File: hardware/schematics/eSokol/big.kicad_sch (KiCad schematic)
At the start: 35 parts, among them J2 MOT_DRV_THR, J3 THR_JACK, J4 THR_JACK, J6 BIGBATT_CHRG, J7 MOT_DRV_THR, M1 MY1016Z2, M2 Fan, Q11 BC547, Q12 S8550, Q13 BC547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

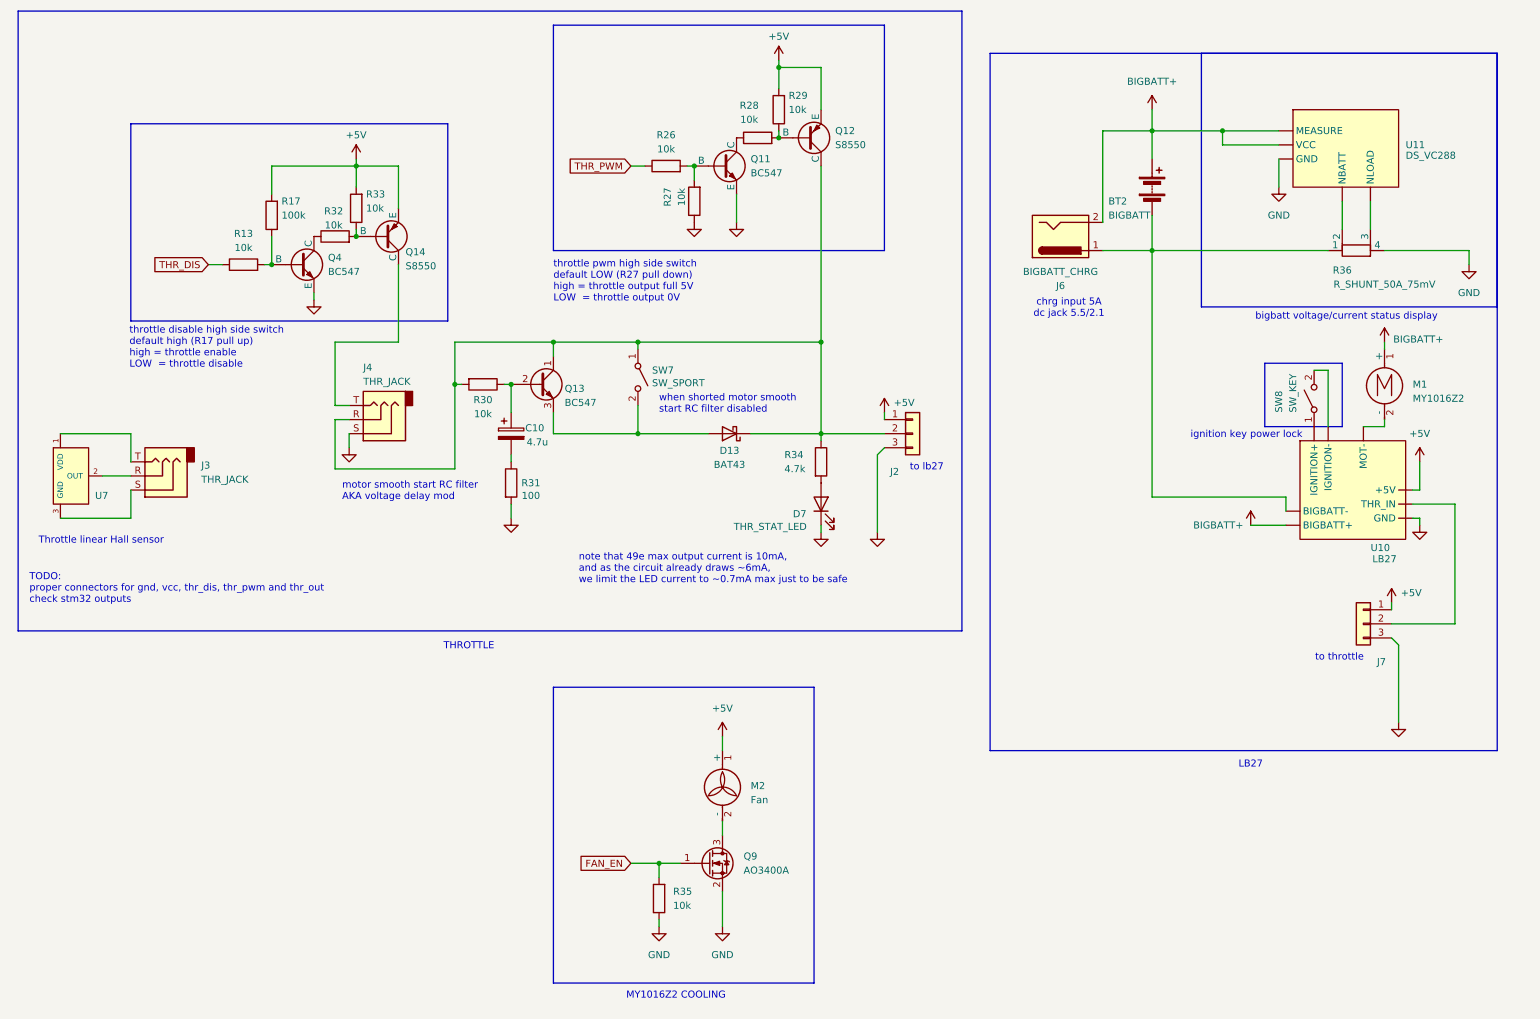
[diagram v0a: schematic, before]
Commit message: Create one BIG schematic containing everything related to motor and its driver
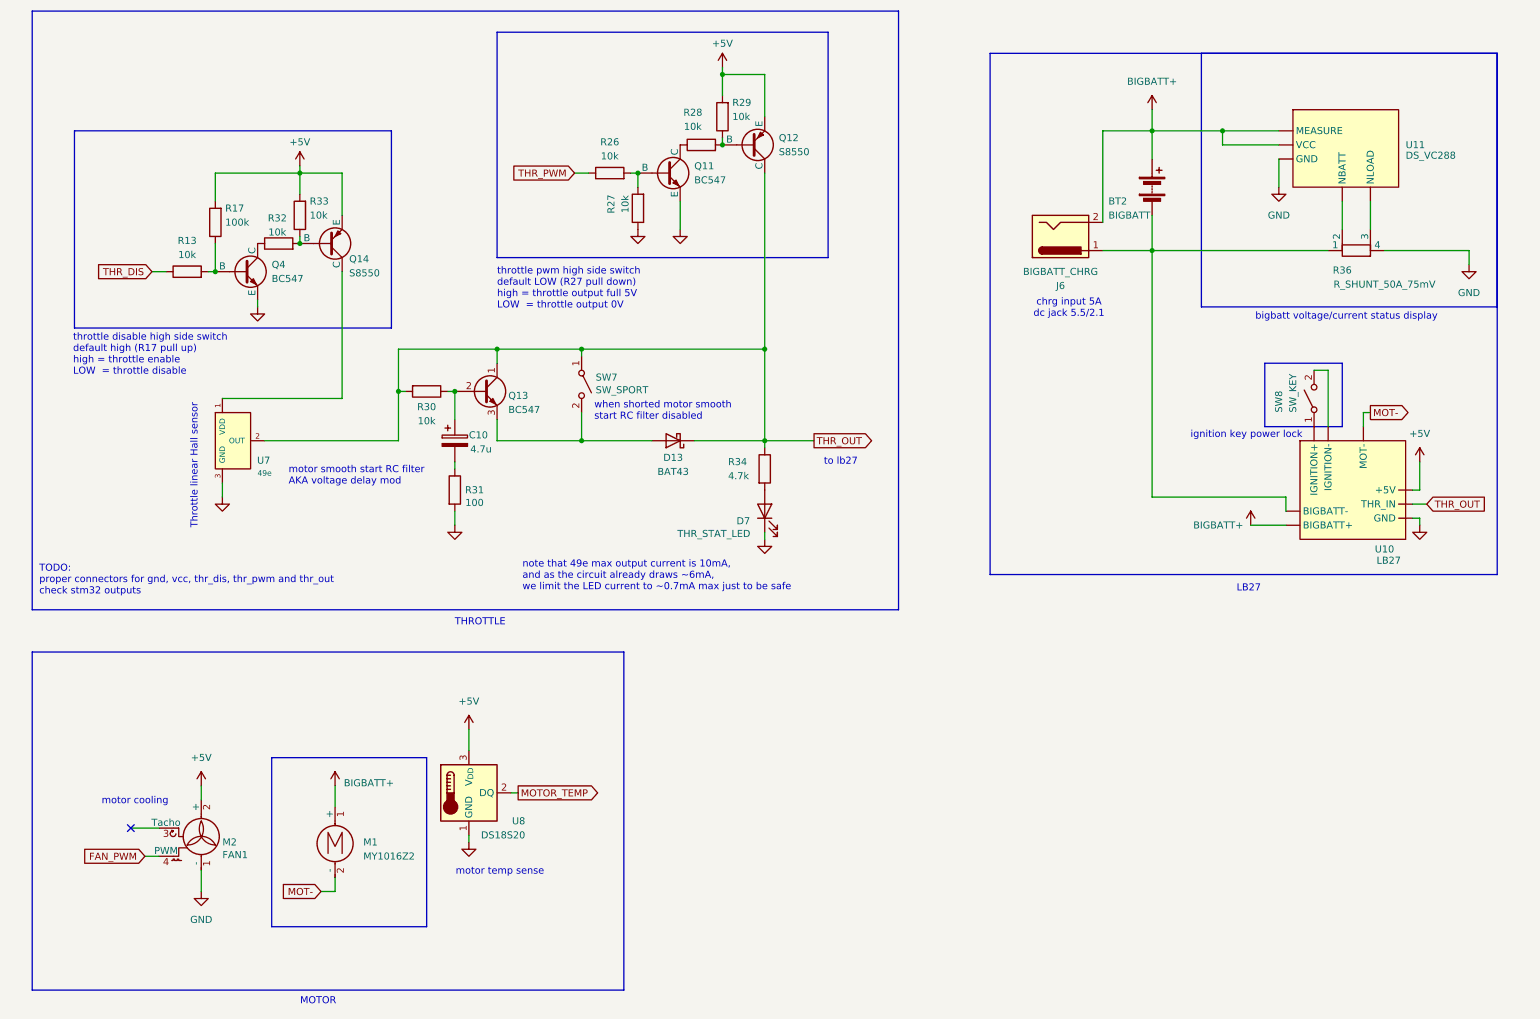
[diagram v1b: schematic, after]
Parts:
- removed J2, J7: MOT_DRV_THR, symbol Connector_Generic:Conn_01x03
- removed J3, J4: THR_JACK, symbol Connector_Audio:AudioJack3
- removed M2: Fan, symbol Motor:Fan
- removed Q9: AO3400A, Package_TO_SOT_SMD:SOT-23, symbol Transistor_FET:AO3400A
- removed R35: 10k, symbol Device:R
- added M2: FAN1, symbol Motor:Fan_4pin
- added U8: DS18S20, Package_TO_SOT_THT:TO-92_Inline, symbol Sensor_Temperature:DS18S20
- U7: value Hall_Sensor -> 49e
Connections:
- net +5V: now also M2.2 (+), U8.3 (V_{DD})
- net GND: now also U7.3 (GND), M2.1 (-), U8.1 (GND)
- net THR_OUT: now reaches D13.1 (K), Q12.1 (C), Q13.1 (C), R30.2, R34.1, SW7.1 (A)
- net THR_OUT: now also U10. (THR_IN), U7.2 (OUT)
- net at Q14.1 (C): now also U7.1 (VDD)
- net MOT-: now reaches M1.2 (-), U10. (THR_IN)
- new net FAN_PWM: M2.4 (PWM)
- new net MOTOR_TEMP: U8.2 (DQ)
- no-connect marks 0 -> 1
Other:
- note added: "MOTOR"
- note added: "motor cooling"
- note added: "motor temp sense"
- note removed: "MY1016Z2 COOLING"
- note removed: "to throttle"
- moved on the sheet: C10, D13, D7, Q11, Q12, Q13, Q14, Q4, R13, R17, R26, R27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

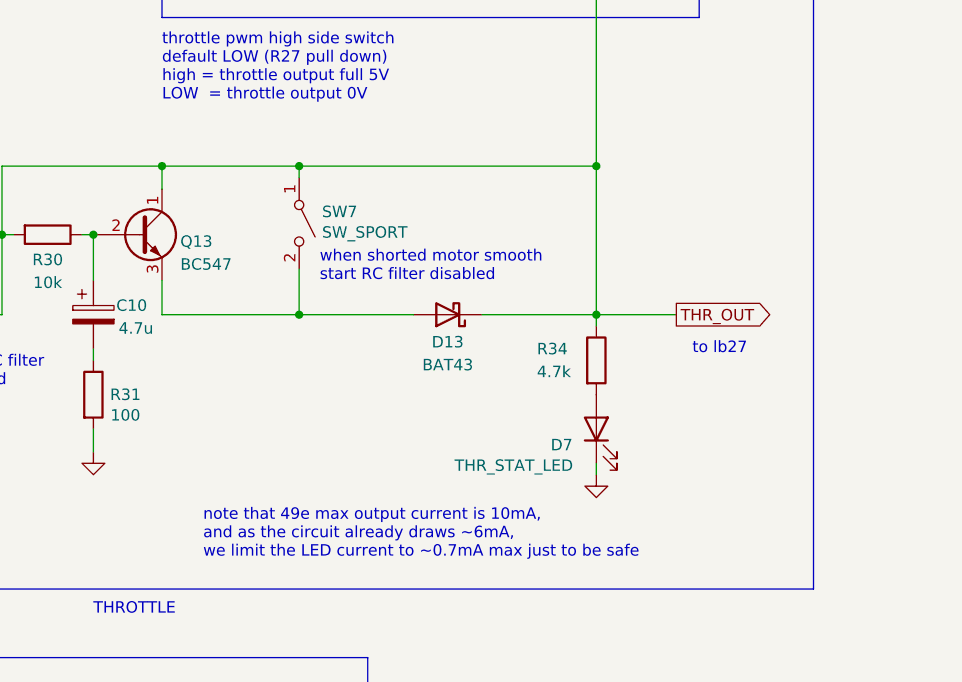
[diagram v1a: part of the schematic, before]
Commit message: schematics: eSokol: big: replace SW_SPORT with digital THR_SPORT input
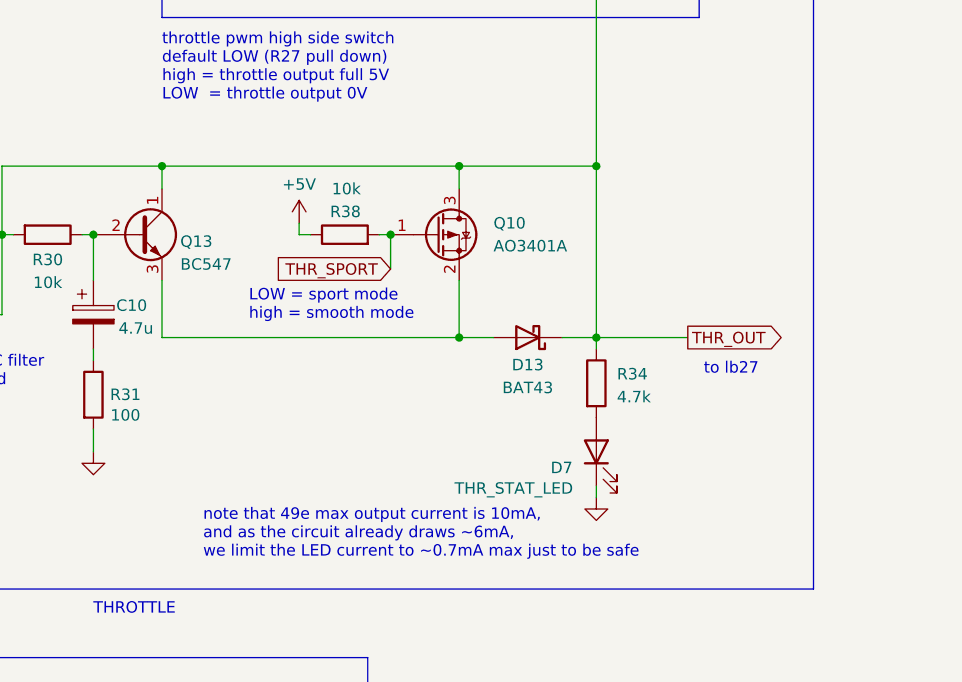
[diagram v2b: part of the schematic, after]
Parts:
- removed SW7: SW_SPORT, Button_Switch_THT:SW_DIP_SPSTx01_Slide_9.78x4.72mm_W7.62mm_P2.54mm, symbol Switch:SW_SPST
- added Q10: AO3401A, Package_TO_SOT_SMD:SOT-23, symbol Transistor_FET:AO3401A
- added R38: 10k, symbol Device:R
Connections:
- net +5V: now also R38.1
- net THR_OUT: now also Q10.3 (D)
- net at D13.2 (A), Q13.3 (E): now also Q10.2 (S)
- new net THR_SPORT: Q10.1 (G), R38.2
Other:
- note added: "LOW = sport mode high = smooth mode"
- note removed: "when shorted motor smooth start RC filter disabled"
- moved on the sheet: D13, D7, R34

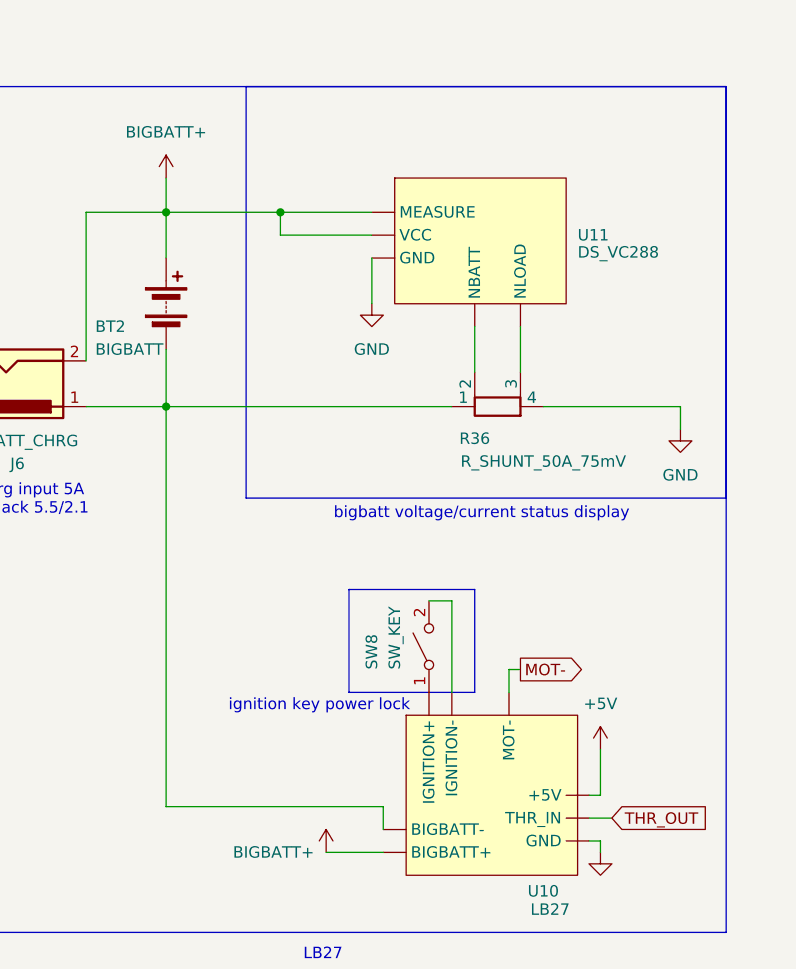
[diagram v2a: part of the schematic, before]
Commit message: hardware/schematics: update mcu and big schematics to reflect current project state
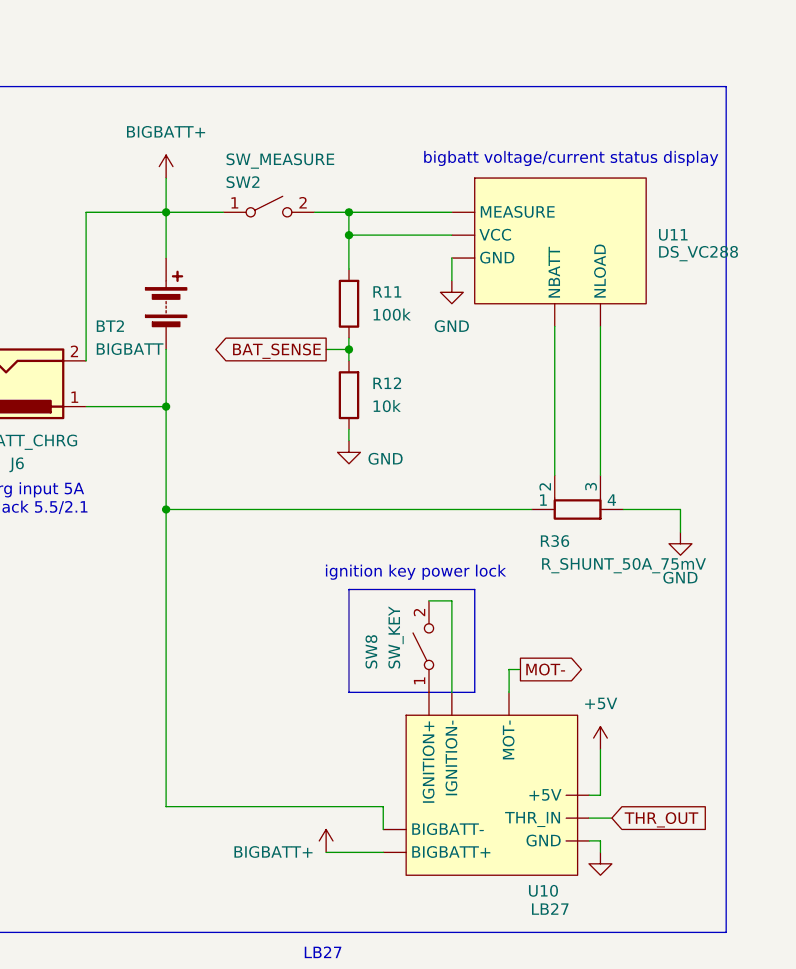
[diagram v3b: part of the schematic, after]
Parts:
- added R11: 100k, symbol Device:R
- added R12: 10k, symbol Device:R
- added SW2: SW_MEASURE, symbol Switch:SW_SPST
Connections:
- net BIGBATT+: now also SW2.1 (A); no longer U11. (VCC)
- net GND: now also R12.1
- new net: R11.2, SW2.2 (B), U11. (VCC)
- new net BAT_SENSE: R11.1, R12.2
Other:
- moved on the sheet: R36, U11

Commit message: WIP: update some schematics to reflect the newest design changes
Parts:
- removed C10: 4.7u, symbol Device:C_Polarized
- removed D13: BAT43, Diode_THT:D_DO-35_SOD27_P7.62mm_Horizontal, symbol Diode:BAT43
- removed D7: THR_STAT_LED, symbol Device:LED
- removed Q10: AO3401A, Package_TO_SOT_SMD:SOT-23, symbol Transistor_FET:AO3401A
- removed Q11, Q4: BC547, symbol Simulation_SPICE:NPN
- removed Q12, Q14: S8550, symbol Simulation_SPICE:PNP
- removed Q13: BC547, Package_TO_SOT_THT:TO-92_Inline, symbol Transistor_BJT:BC547
- removed R13, R26, R27, R28, R29, R30, R32, R33, R38: 10k, symbol Device:R
- removed R17: 100k, symbol Device:R
- removed R31: 100, symbol Device:R
- removed R34: 4.7k, symbol Device:R
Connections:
- net THR_OUT: no longer U7.2 (OUT)
- net 3V3_L: now reaches U7.1 (VDD)
- new net THROTTLE_AIN: U7.2 (OUT)
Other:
- note removed: "LOW = sport mode high = smooth mode"
- note removed: "motor smooth start RC filter AKA voltage delay mod"
- note removed: "note that 49e max output current is 10mA, and as the circuit already draws ~6mA, we limit the LED current to ~0.7mA max just to be safe"
- note removed: "throttle disable high side switch default high (R17 pull up) high = throttle enable LOW = throttle disable"
- note removed: "throttle pwm high side switch default LOW (R27 pull down) high = throttle output full 5V LOW = throttle output 0V"
- note removed: "to lb27"
